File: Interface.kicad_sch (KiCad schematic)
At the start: 20 parts, among them J1 Debugger, J2 USART, J3 SPI, J4 USB_C_Receptacle_USB2.0, Q1 Q_NMOS_GSD, U3 USBLC6-2SC6

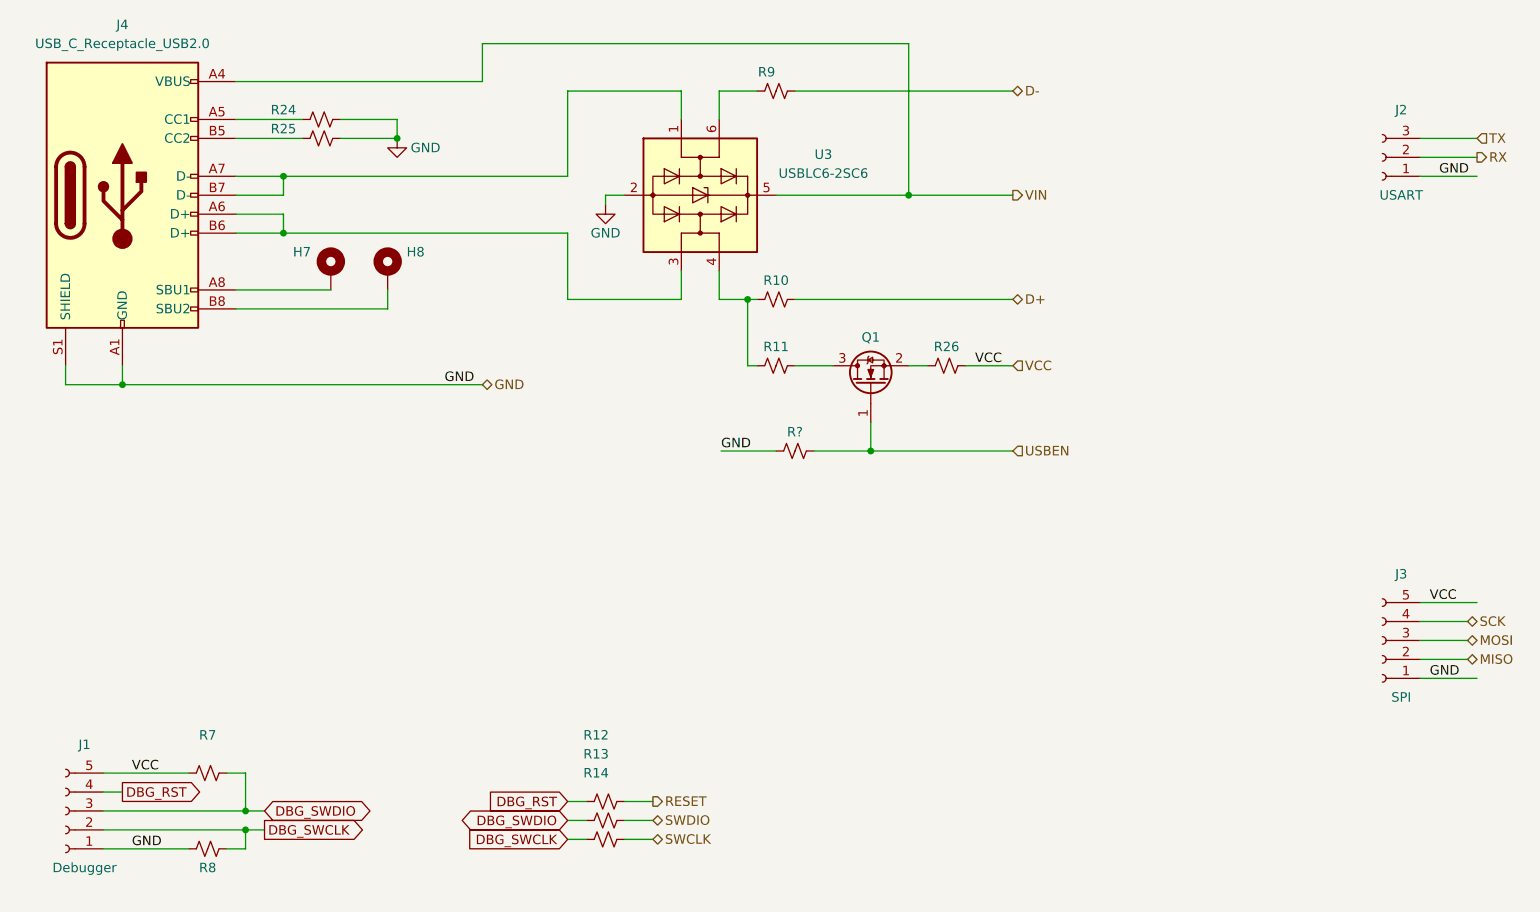
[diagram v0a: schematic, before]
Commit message: modify pcb footprint
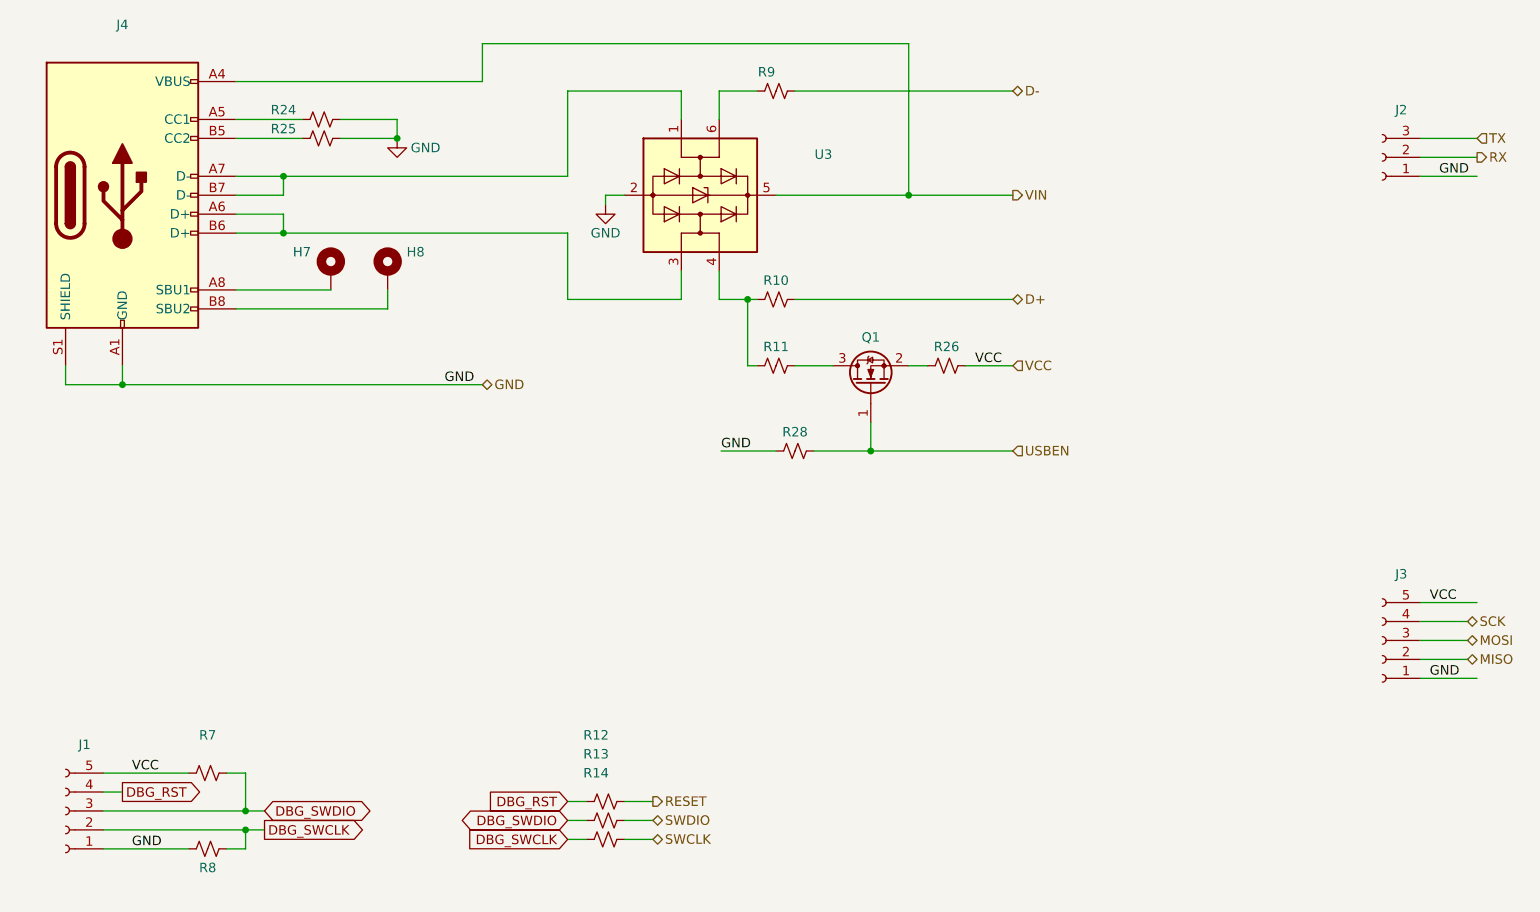
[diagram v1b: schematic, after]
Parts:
- H7, H8: value MountingHole_Pad -> (none); footprint NetTie:NetTie-2_SMD_Pad0.5mm -> (none)
- J1: value Debugger -> (none); footprint Connector_PinHeader_2.00mm:PinHeader_1x05_P2.00mm_Vertical -> (none)
- J2: value USART -> (none); footprint Connector_PinHeader_2.00mm:PinHeader_1x03_P2.00mm_Vertical -> (none)
- J3: value SPI -> (none); footprint Connector_PinHeader_2.00mm:PinHeader_1x05_P2.00mm_Vertical -> (none)
- J4: value USB_C_Receptacle_USB2.0 -> (none); footprint Connector_USB:USB_C_Receptacle_HRO_TYPE-C-31-M-12 -> (none)
- Q1: value Q_NMOS_GSD -> (none); footprint Package_TO_SOT_SMD:SOT-23 -> (none)
- U3: value USBLC6-2SC6 -> (none); footprint Package_TO_SOT_SMD:SOT-23-6 -> (none)
- gave numbers to parts that had none: 1
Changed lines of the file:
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@@
     (in_bom yes) (on_board yes) (fields_autoplaced)
     (property "Reference" "U3" (id 0) (at 149.86 47.8788 90))
-    (property "Value" "USBLC6-2SC6" (id 1) (at 149.86 50.4188 90))
-    (property "Footprint" "Package_TO_SOT_SMD:SOT-23-6" (id 2) (at 120.65 53.34 0)
+    (property "Value" "" (id 1) (at 149.86 50.4188 90))
+    (property "Footprint" "" (id 2) (at 120.65 53.34 0)
       (effects (font (size 1.27 1.27)) hide)
     )
@@
       (effects (font (size 1.27 1.27)) (justify left))
     )
-    (property "Value" "MountingHole_Pad" (id 1) (at 86.36 63.4999 0)
+    (property "Value" "" (id 1) (at 86.36 63.4999 0)
       (effects (font (size 1.27 1.27)) (justify left) hide)
     )
-    (property "Footprint" "NetTie:NetTie-2_SMD_Pad0.5mm" (id 2) (at 83.82 63.5 0)
+    (property "Footprint" "" (id 2) (at 83.82 63.5 0)
       (effects (font (size 1.27 1.27)) hide)
     )
@@
     (in_bom yes) (on_board yes)
     (property "Reference" "J3" (id 0) (at 227.33 104.14 0))
-    (property "Value" "SPI" (id 1) (at 227.33 120.65 0))
-    (property "Footprint" "Connector_PinHeader_2.00mm:PinHeader_1x05_P2.00mm_Vertical" (id 2) (at 224.79 113.03 0)
+    (property "Value" "" (id 1) (at 227.33 120.65 0))
+    (property "Footprint" "" (id 2) (at 224.79 113.03 0)
       (effects (font (size 1.27 1.27)) hide)
     )
@@
     (in_bom yes) (on_board yes)
     (property "Reference" "J1" (id 0) (at 50.8 127 0))
-    (property "Value" "Debugger" (id 1) (at 50.8 143.51 0))
-    (property "Footprint" "Connector_PinHeader_2.00mm:PinHeader_1x05_P2.00mm_Vertical" (id 2) (at 48.26 135.89 0)
+    (property "Value" "" (id 1) (at 50.8 143.51 0))
+    (property "Footprint" "" (id 2) (at 48.26 135.89 0)
       (effects (font (size 1.27 1.27)) hide)
     )
@@
   (symbol (lib_id "Device:R_Small_US") (at 146.05 87.63 90) (unit 1)
     (in_bom yes) (on_board yes)
-    (property "Reference" "R?" (id 0) (at 146.05 85.09 90))
+    (property "Reference" "R28" (id 0) (at 146.05 85.09 90))
     (property "Value" "" (id 1) (at 146.05 90.17 90))
     (property "Footprint" "" (id 2) (at 146.05 87.63 0)
@@
     (in_bom yes) (on_board yes)
     (property "Reference" "J2" (id 0) (at 227.33 41.91 0))
-    (property "Value" "USART" (id 1) (at 227.33 53.34 0))
-    (property "Footprint" "Connector_PinHeader_2.00mm:PinHeader_1x03_P2.00mm_Vertical" (id 2) (at 224.79 48.26 0)
+    (property "Value" "" (id 1) (at 227.33 53.34 0))
+    (property "Footprint" "" (id 2) (at 224.79 48.26 0)
       (effects (font (size 1.27 1.27)) hide)
     )
@@
     (in_bom yes) (on_board yes) (fields_autoplaced)
     (property "Reference" "J4" (id 0) (at 55.88 30.48 0))
-    (property "Value" "USB_C_Receptacle_USB2.0" (id 1) (at 55.88 33.02 0))
-    (property "Footprint" "Connector_USB:USB_C_Receptacle_HRO_TYPE-C-31-M-12" (id 2) (at 59.69 53.34 0)
+    (property "Value" "" (id 1) (at 55.88 33.02 0))
+    (property "Footprint" "" (id 2) (at 59.69 53.34 0)
       (effects (font (size 1.27 1.27)) hide)
     )
@@
     (in_bom yes) (on_board yes)
     (property "Reference" "Q1" (id 0) (at 156.21 72.39 90))
-    (property "Value" "Q_NMOS_GSD" (id 1) (at 156.21 71.12 90)
-      (effects (font (size 1.27 1.27)) hide)
-    )
-    (property "Footprint" "Package_TO_SOT_SMD:SOT-23" (id 2) (at 153.67 73.66 0)
+    (property "Value" "" (id 1) (at 156.21 71.12 90)
+      (effects (font (size 1.27 1.27)) hide)
+    )
+    (property "Footprint" "" (id 2) (at 153.67 73.66 0)
       (effects (font (size 1.27 1.27)) hide)
     )
@@
       (effects (font (size 1.27 1.27)) (justify left))
     )
-    (property "Value" "MountingHole_Pad" (id 1) (at 93.98 63.4999 0)
+    (property "Value" "" (id 1) (at 93.98 63.4999 0)
       (effects (font (size 1.27 1.27)) (justify left) hide)
     )
-    (property "Footprint" "NetTie:NetTie-2_SMD_Pad0.5mm" (id 2) (at 91.44 63.5 0)
-      (effects (font (size 1.27 1.27)) hide)
-    )
+    (property "Footprint" "" (id 2) (at 91.44 63.5 0)
+      (effects (font (size 1.27 1.27)) hide)
+    )
